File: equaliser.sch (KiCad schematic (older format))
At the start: 35 parts

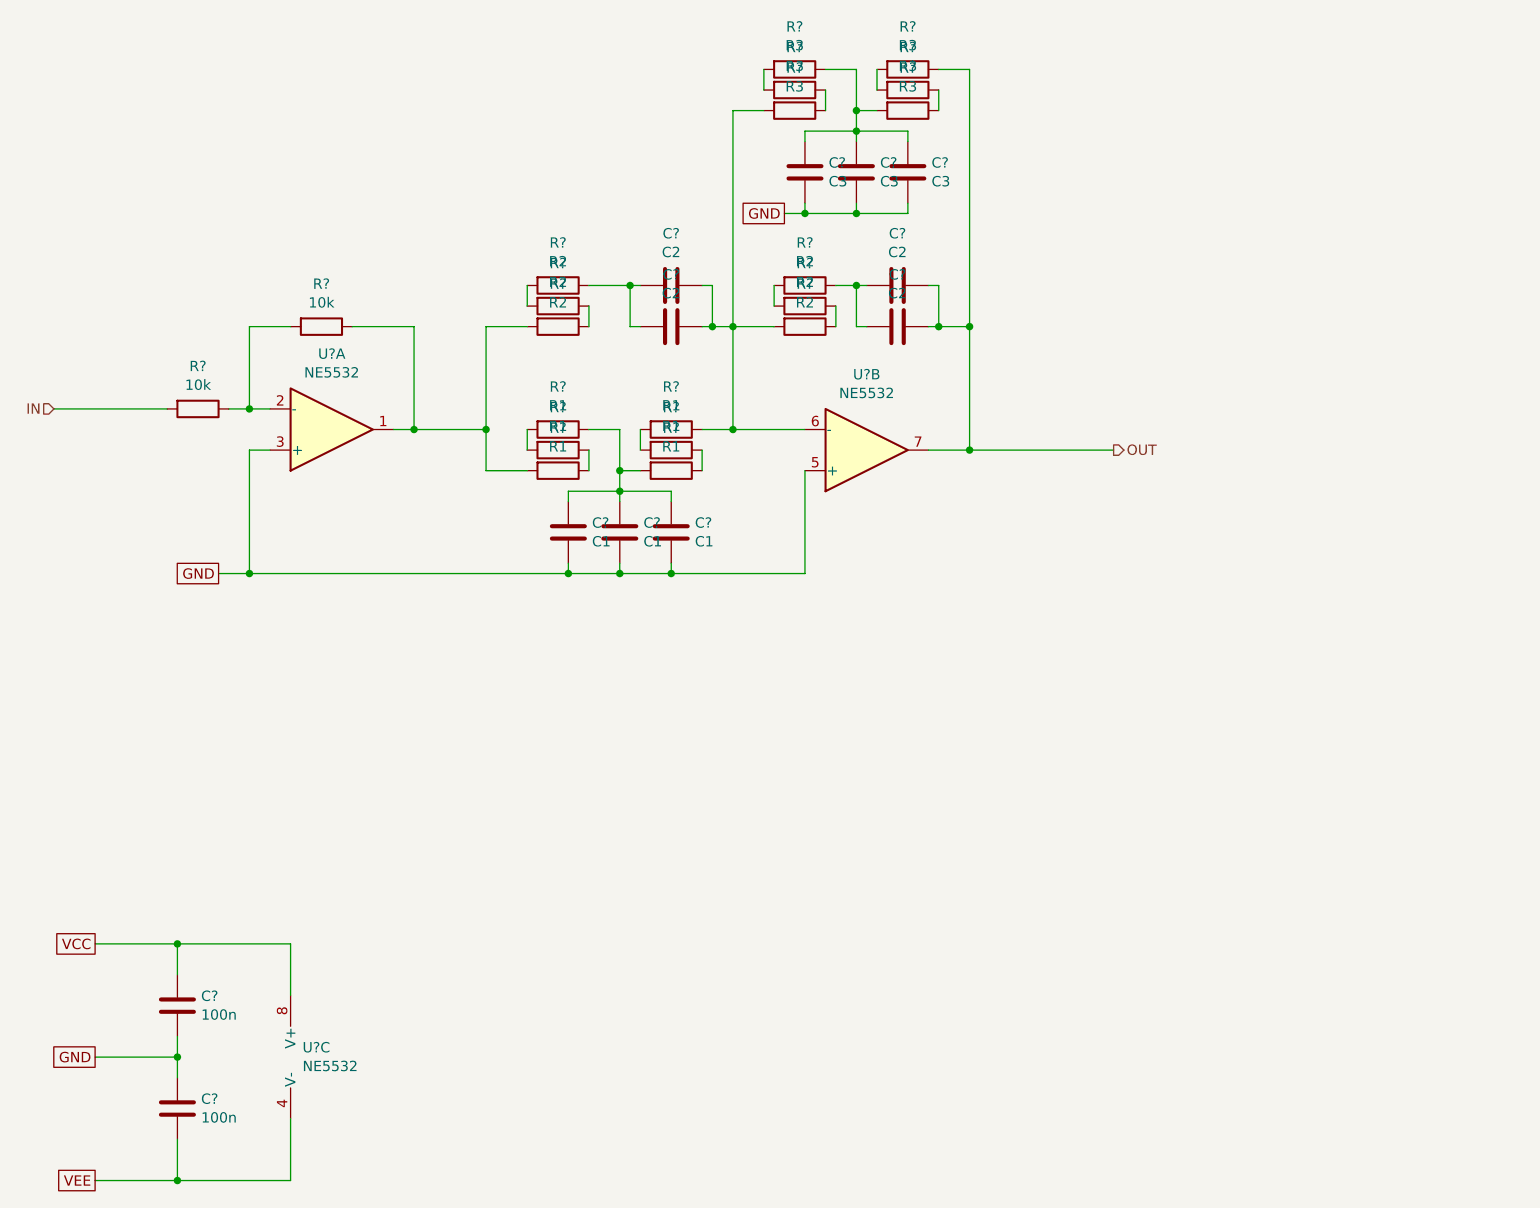
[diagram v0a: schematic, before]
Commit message: improved PSU, gain up front, reordered filter stages, shrunk rumble filter
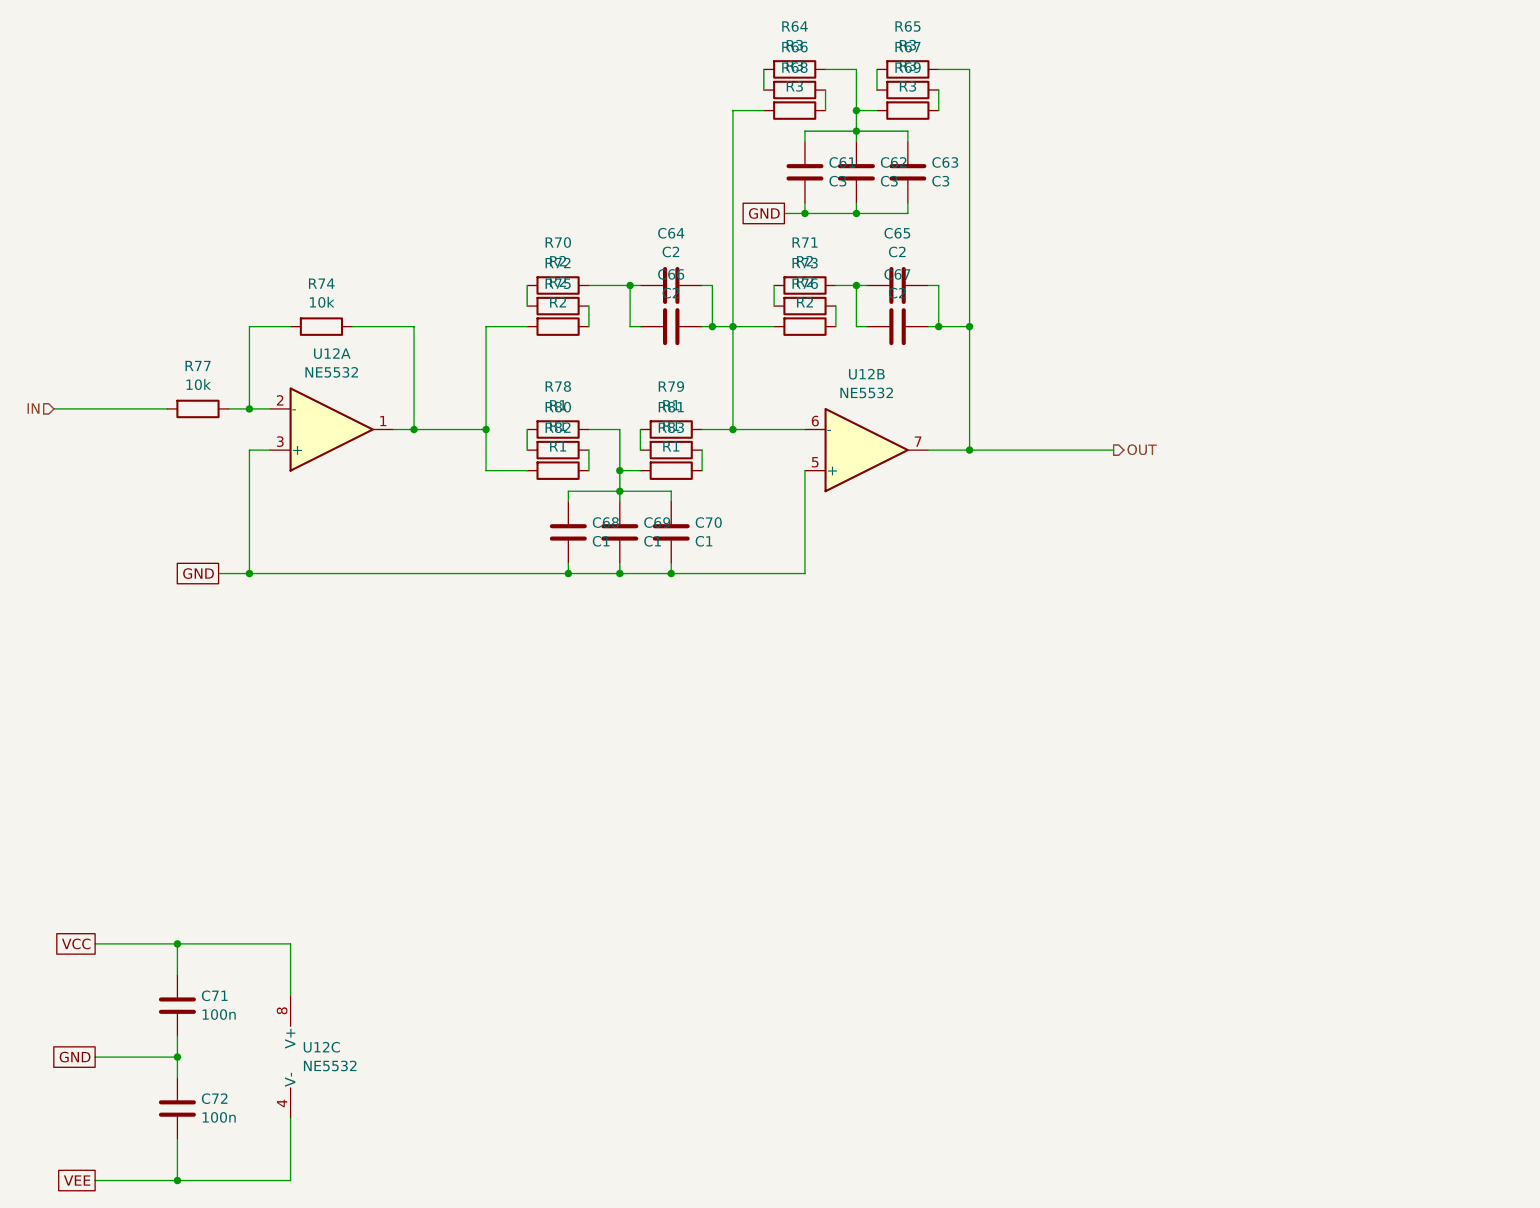
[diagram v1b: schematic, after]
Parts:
- gave numbers to parts that had none: 33
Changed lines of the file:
@@
 AR Path="/61597705/618769AF" Ref="U?"  Part="3"
 AR Path="/615C4B58/618769AF" Ref="U?"  Part="3"
-AR Path="/616914EE/618769AF" Ref="U?"  Part="3"
-F 0 "U?" H 2358 6796 50  0000 L CNN
+AR Path="/616914EE/618769AF" Ref="U12"  Part="3"
+F 0 "U12" H 2358 6796 50  0000 L CNN
 F 1 "NE5532" H 2358 6705 50  0000 L CNN
 F 2 "Housings_DIP:DIP-8_W7.62mm_Socket" H 2400 6750 50  0001 C CNN
@@
 AR Path="/61597705/618769B5" Ref="C?"  Part="1"
 AR Path="/615C4B58/618769B5" Ref="C?"  Part="1"
-AR Path="/616914EE/618769B5" Ref="C?"  Part="1"
-F 0 "C?" H 1865 7046 50  0000 L CNN
+AR Path="/616914EE/618769B5" Ref="C72"  Part="1"
+F 0 "C72" H 1865 7046 50  0000 L CNN
 F 1 "100n" H 1865 6955 50  0000 L CNN
 F 2 "Capacitors_SMD:C_0805" H 1788 6850 50  0001 C CNN
@@
 AR Path="/61597705/618769BB" Ref="C?"  Part="1"
 AR Path="/615C4B58/618769BB" Ref="C?"  Part="1"
-AR Path="/616914EE/618769BB" Ref="C?"  Part="1"
-F 0 "C?" H 1865 6546 50  0000 L CNN
+AR Path="/616914EE/618769BB" Ref="C71"  Part="1"
+F 0 "C71" H 1865 6546 50  0000 L CNN
 F 1 "100n" H 1865 6455 50  0000 L CNN
 F 2 "Capacitors_SMD:C_0805" H 1788 6350 50  0001 C CNN
@@
 Connection ~ 1750 7350
 $Comp
-L Amplifier_Operational:NE5532 U?
+L Amplifier_Operational:NE5532 U12
 U 1 1 61876C74
 P 2500 3700
-F 0 "U?" H 2500 3333 50  0000 C CNN
+F 0 "U12" H 2500 3333 50  0000 C CNN
 F 1 "NE5532" H 2500 3424 50  0000 C CNN
 F 2 "" H 2500 3700 50  0001 C CNN
@@
 $EndComp
 $Comp
-L Amplifier_Operational:NE5532 U?
+L Amplifier_Operational:NE5532 U12
 U 2 1 61877AFD
 P 5100 3800
-F 0 "U?" H 5100 3433 50  0000 C CNN
+F 0 "U12" H 5100 3433 50  0000 C CNN
 F 1 "NE5532" H 5100 3524 50  0000 C CNN
 F 2 "" H 5100 3800 50  0001 C CNN
@@
 $EndComp
 $Comp
-L Device:R R?
+L Device:R R74
 U 1 1 6187BC3E
 P 2450 3200
-F 0 "R?" V 2243 3200 50  0000 C CNN
+F 0 "R74" V 2243 3200 50  0000 C CNN
 F 1 "10k" V 2334 3200 50  0000 C CNN
 F 2 "Resistors_SMD:R_0805" V 2380 3200 50  0001 C CNN
@@
 $EndComp
 $Comp
-L Device:R R?
+L Device:R R77
 U 1 1 6187C5F0
 P 1850 3600
-F 0 "R?" V 1643 3600 50  0000 C CNN
+F 0 "R77" V 1643 3600 50  0000 C CNN
 F 1 "10k" V 1734 3600 50  0000 C CNN
 F 2 "Resistors_SMD:R_0805" V 1780 3600 50  0001 C CNN
@@
 GND
 $Comp
-L Device:R R?
+L Device:R R75
 U 1 1 61887A13
 P 3600 3200
-F 0 "R?" V 3393 3200 50  0000 C CNN
+F 0 "R75" V 3393 3200 50  0000 C CNN
 F 1 "R2" V 3484 3200 50  0000 C CNN
 F 2 "Resistors_SMD:R_0805" V 3530 3200 50  0001 C CNN
@@
 $EndComp
 $Comp
-L Device:R R?
+L Device:R R72
 U 1 1 618881D6
 P 3600 3100
-F 0 "R?" V 3393 3100 50  0000 C CNN
+F 0 "R72" V 3393 3100 50  0000 C CNN
 F 1 "R2" V 3484 3100 50  0000 C CNN
 F 2 "Resistors_SMD:R_0805" V 3530 3100 50  0001 C CNN
@@
 $EndComp
 $Comp
-L Device:R R?
+L Device:R R70
 U 1 1 6188AB3F
 P 3600 3000
-F 0 "R?" V 3393 3000 50  0000 C CNN
+F 0 "R70" V 3393 3000 50  0000 C CNN
 F 1 "R2" V 3484 3000 50  0000 C CNN
 F 2 "Resistors_SMD:R_0805" V 3530 3000 50  0001 C CNN
@@
 $EndComp
 $Comp
-L Device:C C?
+L Device:C C66
 U 1 1 6188B0E8
 P 4150 3200
-F 0 "C?" V 3898 3200 50  0000 C CNN
+F 0 "C66" V 3898 3200 50  0000 C CNN
 F 1 "C2" V 3989 3200 50  0000 C CNN
 F 2 "Capacitors_ThroughHole:C_Rect_L10.0mm_W5.0mm_P5.00mm_P7.50mm" H 4188 3050 50  0001 C CNN
@@
 	3450 3100 3450 3000
 $Comp
-L Device:R R?
+L Device:R R76
 U 1 1 6188EADB
 P 4800 3200
-F 0 "R?" V 4593 3200 50  0000 C CNN
+F 0 "R76" V 4593 3200 50  0000 C CNN
 F 1 "R2" V 4684 3200 50  0000 C CNN
 F 2 "Resistors_SMD:R_0805" V 4730 3200 50  0001 C CNN
@@
 $EndComp
 $Comp
-L Device:R R?
+L Device:R R73
 U 1 1 6188EAE1
 P 4800 3100
-F 0 "R?" V 4593 3100 50  0000 C CNN
+F 0 "R73" V 4593 3100 50  0000 C CNN
 F 1 "R2" V 4684 3100 50  0000 C CNN
 F 2 "Resistors_SMD:R_0805" V 4730 3100 50  0001 C CNN
@@
 $EndComp
 $Comp
-L Device:R R?
+L Device:R R71
 U 1 1 6188EAE7
 P 4800 3000
-F 0 "R?" V 4593 3000 50  0000 C CNN
+F 0 "R71" V 4593 3000 50  0000 C CNN
 F 1 "R2" V 4684 3000 50  0000 C CNN
 F 2 "Resistors_SMD:R_0805" V 4730 3000 50  0001 C CNN
@@
 $EndComp
 $Comp
-L Device:C C?
+L Device:C C67
 U 1 1 6188EAED
 P 5250 3200
-F 0 "C?" V 4998 3200 50  0000 C CNN
+F 0 "C67" V 4998 3200 50  0000 C CNN
 F 1 "C2" V 5089 3200 50  0000 C CNN
 F 2 "Capacitors_ThroughHole:C_Rect_L10.0mm_W5.0mm_P5.00mm_P7.50mm" H 5288 3050 50  0001 C CNN
@@
 	4950 3000 5050 3000
 $Comp
-L Device:R R?
+L Device:R R82
 U 1 1 61891898
 P 3600 3900
-F 0 "R?" V 3393 3900 50  0000 C CNN
+F 0 "R82" V 3393 3900 50  0000 C CNN
 F 1 "R1" V 3484 3900 50  0000 C CNN
 F 2 "Resistors_SMD:R_0805" V 3530 3900 50  0001 C CNN
@@
 $EndComp
 $Comp
-L Device:R R?
+L Device:R R80
 U 1 1 6189189E
 P 3600 3800
-F 0 "R?" V 3393 3800 50  0000 C CNN
+F 0 "R80" V 3393 3800 50  0000 C CNN
 F 1 "R1" V 3484 3800 50  0000 C CNN
 F 2 "Resistors_SMD:R_0805" V 3530 3800 50  0001 C CNN
@@
 $EndComp
 $Comp
-L Device:R R?
+L Device:R R78
 U 1 1 618918A4
 P 3600 3700
-F 0 "R?" V 3393 3700 50  0000 C CNN
+F 0 "R78" V 3393 3700 50  0000 C CNN
 F 1 "R1" V 3484 3700 50  0000 C CNN
 F 2 "Resistors_SMD:R_0805" V 3530 3700 50  0001 C CNN
@@
 	3450 3800 3450 3700
 $Comp
-L Device:R R?
+L Device:R R83
 U 1 1 61893819
 P 4150 3900
-F 0 "R?" V 3943 3900 50  0000 C CNN
+F 0 "R83" V 3943 3900 50  0000 C CNN
 F 1 "R1" V 4034 3900 50  0000 C CNN
 F 2 "Resistors_SMD:R_0805" V 4080 3900 50  0001 C CNN
@@
 $EndComp
 $Comp
-L Device:R R?
+L Device:R R81
 U 1 1 6189381F
 P 4150 3800
-F 0 "R?" V 3943 3800 50  0000 C CNN
+F 0 "R81" V 3943 3800 50  0000 C CNN
 F 1 "R1" V 4034 3800 50  0000 C CNN
 F 2 "Resistors_SMD:R_0805" V 4080 3800 50  0001 C CNN
@@
 $EndComp
 $Comp
-L Device:R R?
+L Device:R R79
 U 1 1 61893825
 P 4150 3700
-F 0 "R?" V 3943 3700 50  0000 C CNN
+F 0 "R79" V 3943 3700 50  0000 C CNN
 F 1 "R1" V 4034 3700 50  0000 C CNN
 F 2 "Resistors_SMD:R_0805" V 4080 3700 50  0001 C CNN
@@
 	4300 3200 4350 3200
 $Comp
-L Device:C C?
+L Device:C C68
 U 1 1 6189B712
 P 3650 4200
-F 0 "C?" H 3765 4246 50  0000 L CNN
+F 0 "C68" H 3765 4246 50  0000 L CNN
 F 1 "C1" H 3765 4155 50  0000 L CNN
 F 2 "Capacitors_ThroughHole:C_Rect_L10.0mm_W5.0mm_P5.00mm_P7.50mm" H 3688 4050 50  0001 C CNN
@@
 	5600 3800 5400 3800
 $Comp
-L Device:R R?
+L Device:R R68
 U 1 1 618B4E04
 P 4750 2150
-F 0 "R?" V 4543 2150 50  0000 C CNN
+F 0 "R68" V 4543 2150 50  0000 C CNN
 F 1 "R3" V 4634 2150 50  0000 C CNN
 F 2 "Resistors_SMD:R_0805" V 4680 2150 50  0001 C CNN
@@
 $EndComp
 $Comp
-L Device:R R?
+L Device:R R66
 U 1 1 618B4E0A
 P 4750 2050
-F 0 "R?" V 4543 2050 50  0000 C CNN
+F 0 "R66" V 4543 2050 50  0000 C CNN
 F 1 "R3" V 4634 2050 50  0000 C CNN
 F 2 "Resistors_SMD:R_0805" V 4680 2050 50  0001 C CNN
@@
 $EndComp
 $Comp
-L Device:R R?
+L Device:R R64
 U 1 1 618B4E10
 P 4750 1950
-F 0 "R?" V 4543 1950 50  0000 C CNN
+F 0 "R64" V 4543 1950 50  0000 C CNN
 F 1 "R3" V 4634 1950 50  0000 C CNN
 F 2 "Resistors_SMD:R_0805" V 4680 1950 50  0001 C CNN
@@
 	4600 2050 4600 1950
 $Comp
-L Device:R R?
+L Device:R R69
 U 1 1 618B4E18
 P 5300 2150
-F 0 "R?" V 5093 2150 50  0000 C CNN
+F 0 "R69" V 5093 2150 50  0000 C CNN
 F 1 "R3" V 5184 2150 50  0000 C CNN
 F 2 "Resistors_SMD:R_0805" V 5230 2150 50  0001 C CNN
@@
 $EndComp
 $Comp
-L Device:R R?
+L Device:R R67
 U 1 1 618B4E1E
 P 5300 2050
-F 0 "R?" V 5093 2050 50  0000 C CNN
+F 0 "R67" V 5093 2050 50  0000 C CNN
 F 1 "R3" V 5184 2050 50  0000 C CNN
 F 2 "Resistors_SMD:R_0805" V 5230 2050 50  0001 C CNN
@@
 $EndComp
 $Comp
-L Device:R R?
+L Device:R R65
 U 1 1 618B4E24
 P 5300 1950
-F 0 "R?" V 5093 1950 50  0000 C CNN
+F 0 "R65" V 5093 1950 50  0000 C CNN
 F 1 "R3" V 5184 1950 50  0000 C CNN
 F 2 "Resistors_SMD:R_0805" V 5230 1950 50  0001 C CNN
@@
 Connection ~ 5050 2150
 $Comp
-L Device:C C?
+L Device:C C61
 U 1 1 618B4E39
 P 4800 2450
-F 0 "C?" H 4915 2496 50  0000 L CNN
+F 0 "C61" H 4915 2496 50  0000 L CNN
 F 1 "C3" H 4915 2405 50  0000 L CNN
 F 2 "Capacitors_ThroughHole:C_Rect_L10.0mm_W5.0mm_P5.00mm_P7.50mm" H 4838 2300 50  0001 C CNN
@@
 	5400 3200 5450 3200
 $Comp
-L Device:C C?
+L Device:C C64
 U 1 1 6191FC2F
 P 4150 3000
-F 0 "C?" V 3898 3000 50  0000 C CNN
+F 0 "C64" V 3898 3000 50  0000 C CNN
 F 1 "C2" V 3989 3000 50  0000 C CNN
 F 2 "Capacitors_SMD:C_1210_HandSoldering" H 4188 2850 50  0001 C CNN
@@
 $EndComp
 $Comp
-L Device:C C?
+L Device:C C65
 U 1 1 61925A41
 P 5250 3000
-F 0 "C?" V 4998 3000 50  0000 C CNN
+F 0 "C65" V 4998 3000 50  0000 C CNN
 F 1 "C2" V 5089 3000 50  0000 C CNN
 F 2 "Capacitors_SMD:C_1210_HandSoldering" H 5288 2850 50  0001 C CNN
@@
 	5450 3200 5600 3200
 $Comp
-L Device:C C?
+L Device:C C69
 U 1 1 6193AE35
 P 3900 4200
-F 0 "C?" H 4015 4246 50  0000 L CNN
+F 0 "C69" H 4015 4246 50  0000 L CNN
 F 1 "C1" H 4015 4155 50  0000 L CNN
 F 2 "Capacitors_ThroughHole:C_Rect_L10.0mm_W5.0mm_P5.00mm_P7.50mm" H 3938 4050 50  0001 C CNN
@@
 $EndComp
 $Comp
-L Device:C C?
+L Device:C C70
 U 1 1 6193B2A1
 P 4150 4200
-F 0 "C?" H 4265 4246 50  0000 L CNN
+F 0 "C70" H 4265 4246 50  0000 L CNN
 F 1 "C1" H 4265 4155 50  0000 L CNN
 F 2 "Capacitors_ThroughHole:C_Rect_L10.0mm_W5.0mm_P5.00mm_P7.50mm" H 4188 4050 50  0001 C CNN
@@
 $EndComp
 $Comp
-L Device:C C?
+L Device:C C62
 U 1 1 6193C1FB
 P 5050 2450
-F 0 "C?" H 5165 2496 50  0000 L CNN
+F 0 "C62" H 5165 2496 50  0000 L CNN
 F 1 "C3" H 5165 2405 50  0000 L CNN
 F 2 "Capacitors_ThroughHole:C_Rect_L10.0mm_W5.0mm_P5.00mm_P7.50mm" H 5088 2300 50  0001 C CNN
@@
 $EndComp
 $Comp
-L Device:C C?
+L Device:C C63
 U 1 1 6193C690
 P 5300 2450
-F 0 "C?" H 5415 2496 50  0000 L CNN
+F 0 "C63" H 5415 2496 50  0000 L CNN
 F 1 "C3" H 5415 2405 50  0000 L CNN
 F 2 "Capacitors_ThroughHole:C_Rect_L10.0mm_W5.0mm_P5.00mm_P7.50mm" H 5338 2300 50  0001 C CNN
